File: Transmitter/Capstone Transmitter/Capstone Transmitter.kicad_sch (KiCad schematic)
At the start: 38 parts, among them J1 Conn_01x04, J2 Conn_01x04, J3 Conn_01x02_Socket, J4 Conn_01x02_Socket, J5 Conn_01x02_Socket, J6 AnalogStick Pot1 +/-, J7 AnalogStick Pot2 +/-, Q1 RevPolProt, U2 TPS63020DSJR, U3 ESP32-WROOM-32UE

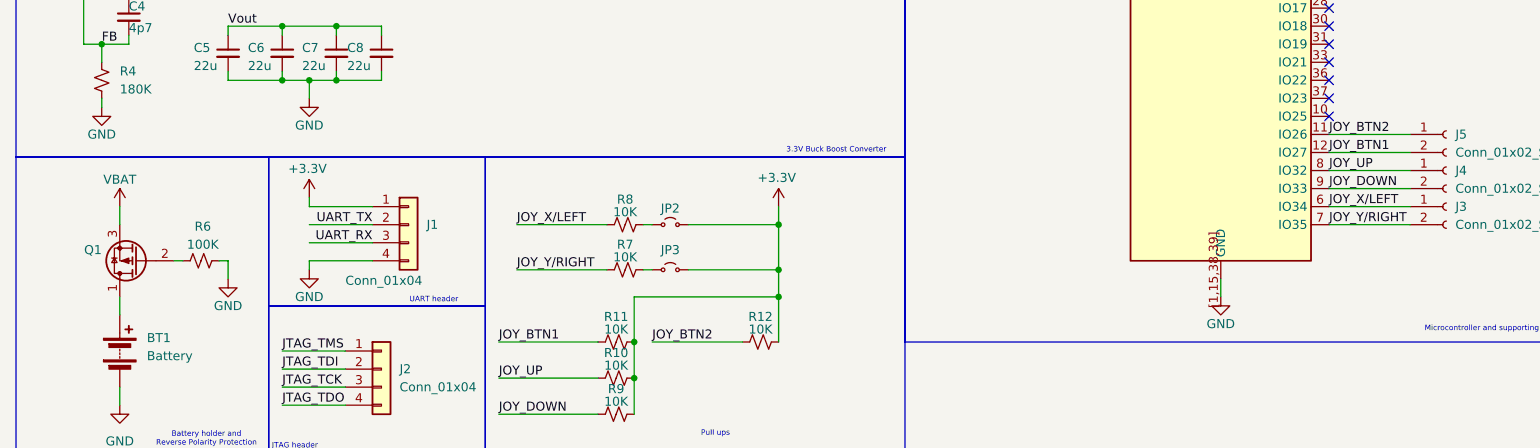
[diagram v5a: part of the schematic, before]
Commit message: Started PCB design with complete transmitter board. Please review
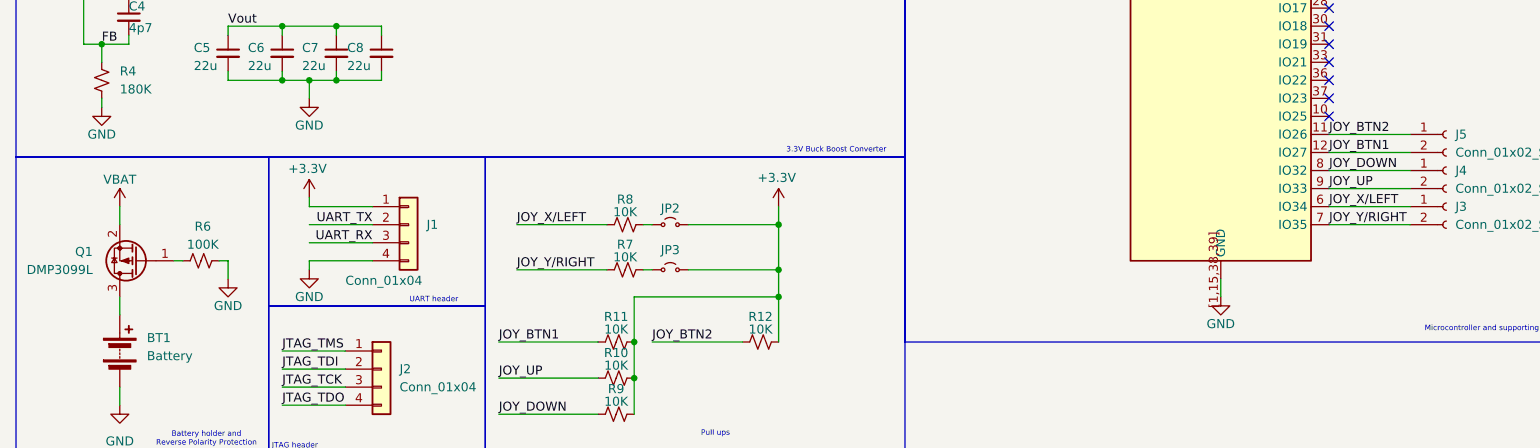
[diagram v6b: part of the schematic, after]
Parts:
- removed Q1: RevPolProt, symbol Transistor_FET:Q_PMOS_DGS
- added Q1: DMP3099L, Package_TO_SOT_SMD:SOT-23, symbol Transistor_FET:DMP3099L
- C1, C10, C11, C2, C4, C5, C6, C7, C8: footprint (none) -> Capacitor_SMD:C_0603_1608Metric
- C3, C9: footprint (none) -> Capacitor_SMD:C_0402_1005Metric
- J1, J2: footprint (none) -> Connector_PinHeader_2.54mm:PinHeader_1x04_P2.54mm_Vertical
- J3, J4, J5, J6, J7: footprint (none) -> TerminalBlock_CUI:TerminalBlock_CUI_TB007-508-02_1x02_P5.08mm_Horizontal
- JP1, JP2, JP3: footprint (none) -> Connector_PinHeader_2.54mm:PinHeader_1x02_P2.54mm_Vertical
- L1: footprint (none) -> Inductor_SMD_Wurth:L_Wurth_WE-LQSH-4020
- R1, R10, R11, R12, R2, R3, R4, R5, R6, R7, R8, R9: footprint (none) -> Resistor_SMD:R_0603_1608Metric
- U2: footprint DSJ14_2P85X1P58 -> footprints:DSJ14_2P85X1P58
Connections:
- net JOY_DOWN: now also J4.1 (Pin_1), U3.8 (IO32); no longer J4.2 (Pin_2), U3.9 (IO33)
- net JOY_UP: now also J4.2 (Pin_2), U3.9 (IO33); no longer J4.1 (Pin_1), U3.8 (IO32)
- net VBAT: now also Q1.2 (S)
- net at BT1.1 (+): now also Q1.3 (D)
- net at R6.1: now also Q1.1 (G)
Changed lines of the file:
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@@
 		)
 	)
-	(label "JOY_UP"
+	(label "JOY_DOWN"
 		(at 196.85 80.01 0)
 		(effects
@@
 		)
 	)
-	(label "JOY_DOWN"
+	(label "JOY_UP"
 		(at 196.85 82.55 0)
 		(effects
@@
 			)
 		)
-		(property "Footprint" ""
+		(property "Footprint" "Capacitor_SMD:C_0603_1608Metric"
 			(at 157.48 33.02 0)
 			(hide yes)
@@
 			)
 		)
-		(property "Footprint" ""
+		(property "Footprint" "TerminalBlock_CUI:TerminalBlock_CUI_TB007-508-02_1x02_P5.08mm_Horizontal"
 			(at 27.94 124.46 0)
 			(hide yes)
@@
 			)
 		)
-		(property "Footprint" ""
+		(property "Footprint" "Capacitor_SMD:C_0402_1005Metric"
 			(at 142.24 21.59 0)
 			(hide yes)
@@
 			)
 		)
-		(property "Footprint" ""
+		(property "Footprint" "Capacitor_SMD:C_0603_1608Metric"
 			(at 49.53 63.5 0)
 			(hide yes)
@@
 			)
 		)
-		(property "Footprint" ""
+		(property "Footprint" "Capacitor_SMD:C_0402_1005Metric"
 			(at 24.13 31.75 0)
 			(hide yes)
@@
 			)
 		)
-		(property "Footprint" ""
+		(property "Footprint" "Capacitor_SMD:C_0603_1608Metric"
 			(at 63.5 63.5 0)
 			(hide yes)
@@
 			)
 		)
-		(property "Footprint" ""
+		(property "Footprint" "Resistor_SMD:R_0603_1608Metric"
 			(at 96.52 109.22 0)
 			(hide yes)
@@
 			)
 		)
-		(property "Footprint" ""
+		(property "Footprint" "Connector_PinHeader_2.54mm:PinHeader_1x04_P2.54mm_Vertical"
 			(at 63.5 107.95 0)
 			(hide yes)
@@
 			)
 		)
-		(property "Footprint" ""
+		(property "Footprint" "TerminalBlock_CUI:TerminalBlock_CUI_TB007-508-02_1x02_P5.08mm_Horizontal"
 			(at 213.36 80.01 0)
 			(hide yes)
@@
 			)
 		)
-		(property "Footprint" ""
+		(property "Footprint" "Connector_PinHeader_2.54mm:PinHeader_1x02_P2.54mm_Vertical"
 			(at 104.14 87.63 0)
 			(hide yes)
@@
 			)
 		)
-		(property "Footprint" ""
+		(property "Footprint" "Connector_PinHeader_2.54mm:PinHeader_1x02_P2.54mm_Vertical"
 			(at 209.55 29.21 0)
 			(hide yes)
@@
 	)
 	(symbol
-		(lib_id "Transistor_FET:Q_PMOS_DGS")
-		(at 29.21 92.71 180)
-		(unit 1)
-		(body_style 1)
-		(exclude_from_sim no)
-		(in_bom yes)
-		(on_board yes)
-		(in_pos_files yes)
-		(dnp no)
-		(property "Reference" "Q1"
-			(at 24.13 91.186 0)
-			(show_name no)
-			(do_not_autoplace no)
-			(effects
-				(font
-					(size 1.27 1.27)
-				)
-				(justify left)
-			)
-		)
-		(property "Value" "RevPolProt"
-			(at 23.876 92.964 0)
-			(hide yes)
-			(show_name no)
-			(do_not_autoplace no)
-			(effects
-				(font
-					(size 1.27 1.27)
-				)
-				(justify left)
-			)
-		)
-		(property "Footprint" ""
-			(at 24.13 95.25 0)
-			(hide yes)
-			(show_name no)
-			(do_not_autoplace no)
-			(effects
-				(font
-					(size 1.27 1.27)
-				)
-			)
-		)
-		(property "Datasheet" ""
-			(at 29.21 92.71 0)
-			(hide yes)
-			(show_name no)
-			(do_not_autoplace no)
-			(effects
-				(font
-					(size 1.27 1.27)
-				)
-			)
-		)
-		(property "Description" "P-MOSFET transistor, drain/gate/source"
-			(at 29.21 92.71 0)
-			(hide yes)
-			(show_name no)
-			(do_not_autoplace no)
-			(effects
-				(font
-					(size 1.27 1.27)
-				)
-			)
-		)
-		(pin "2"
-		)
-		(pin "3"
-		)
-		(pin "1"
-		)
-		(instances
-			(project "Capstone Transmitter"
-				(path "/c6281f45-9be9-4db0-bb6a-14da59dc6c3d"
-					(reference "Q1")
-					(unit 1)
-				)
-			)
-		)
-	)
-	(symbol
 		(lib_id "power:+3.3V")
 		(at 20.32 123.19 0)
@@
 			)
 		)
-		(property "Footprint" ""
+		(property "Footprint" "Resistor_SMD:R_0603_1608Metric"
 			(at 27.94 50.8 0)
 			(hide yes)
@@
 			)
 		)
-		(property "Footprint" ""
+		(property "Footprint" "Inductor_SMD_Wurth:L_Wurth_WE-LQSH-4020"
 			(at 71.12 55.88 0)
 			(hide yes)
@@
 			)
 		)
-		(property "Footprint" ""
+		(property "Footprint" "Capacitor_SMD:C_0603_1608Metric"
 			(at 27.94 58.42 0)
 			(hide yes)
@@
 			)
 		)
-		(property "Footprint" ""
+		(property "Footprint" "Resistor_SMD:R_0603_1608Metric"
 			(at 24.13 67.31 0)
 			(hide yes)
@@
 			)
 		)
-		(property "Footprint" ""
+		(property "Footprint" "Resistor_SMD:R_0603_1608Metric"
 			(at 21.59 50.8 0)
 			(hide yes)
@@
 			)
 		)
-		(property "Footprint" ""
+		(property "Footprint" "Resistor_SMD:R_0603_1608Metric"
 			(at 96.52 114.3 0)
 			(hide yes)
@@
 			)
 		)
-		(property "Footprint" ""
+		(property "Footprint" "Resistor_SMD:R_0603_1608Metric"
 			(at 97.79 87.63 0)
 			(hide yes)
@@
 			)
 		)
-		(property "Footprint" ""
+		(property "Footprint" "Connector_PinHeader_2.54mm:PinHeader_1x02_P2.54mm_Vertical"
 			(at 104.14 93.98 0)
 			(hide yes)
@@
 	)
 	(symbol
+		(lib_id "Transistor_FET:DMP3099L")
+		(at 29.21 92.71 180)
+		(unit 1)
+		(body_style 1)
+		(exclude_from_sim no)
+		(in_bom yes)
+		(on_board yes)
+		(in_pos_files yes)
+		(dnp no)
+		(fields_autoplaced yes)
+		(property "Reference" "Q1"
+			(at 22.86 91.4399 0)
+			(show_name no)
+			(do_not_autoplace no)
+			(effects
+				(font
+					(size 1.27 1.27)
+				)
+				(justify left)
+			)
+		)
+		(property "Value" "DMP3099L"
+			(at 22.86 93.9799 0)
+			(show_name no)
+			(do_not_autoplace no)
+			(effects
+				(font
+					(size 1.27 1.27)
+				)
+				(justify left)
+			)
+		)
+		(property "Footprint" "Package_TO_SOT_SMD:SOT-23"
+			(at 24.13 90.805 0)
+			(hide yes)
+			(show_name no)
+			(do_not_autoplace no)
+			(effects
+				(font
+					(size 1.27 1.27)
+					(italic yes)
+				)
+				(justify left)
+			)
+		)
+		(property "Datasheet" "https://www.diodes.com/assets/Datasheets/DMP3099L.pdf"
+			(at 24.13 88.9 0)
+			(hide yes)
+			(show_name no)
+			(do_not_autoplace no)
+			(effects
+				(font
+					(size 1.27 1.27)
+				)
+				(justify left)
+			)
+		)
+		(property "Description" "-3.8A Id, -30V Vds, P-Channel MOSFET, SOT-23"
+			(at 29.21 92.71 0)
+			(hide yes)
+			(show_name no)
+			(do_not_autoplace no)
+			(effects
+				(font
+					(size 1.27 1.27)
+				)
+			)
+		)
+		(pin "1"
+		)
+		(pin "2"
+		)
+		(pin "3"
+		)
+		(instances
+			(project "Capstone Transmitter"
+				(path "/c6281f45-9be9-4db0-bb6a-14da59dc6c3d"
+					(reference "Q1")
+					(unit 1)
+				)
+			)
+		)
+	)
+	(symbol
 		(lib_id "power:+3.3V")
 		(at 27.94 46.99 0)
@@
 			)
 		)
-		(property "Footprint" ""
+		(property "Footprint" "TerminalBlock_CUI:TerminalBlock_CUI_TB007-508-02_1x02_P5.08mm_Horizontal"
 			(at 213.36 85.09 0)
 			(hide yes)
@@
 			)
 		)
-		(property "Footprint" ""
+		(property "Footprint" "Resistor_SMD:R_0603_1608Metric"
 			(at 96.52 104.14 0)
 			(hide yes)
@@
 			)
 		)
-		(property "Footprint" ""
+		(property "Footprint" "Resistor_SMD:R_0603_1608Metric"
 			(at 38.1 92.71 0)
 			(hide yes)
@@
 			)
 		)
-		(property "Footprint" ""
+		(property "Footprint" "Capacitor_SMD:C_0603_1608Metric"
 			(at 41.91 63.5 0)
 			(hide yes)
@@
 			)
 		)
-		(property "Footprint" ""
+		(property "Footprint" "TerminalBlock_CUI:TerminalBlock_CUI_TB007-508-02_1x02_P5.08mm_Horizontal"
 			(at 27.94 132.08 0)
 			(hide yes)
@@
 			)
 		)
-		(property "Footprint" ""
+		(property "Footprint" "Connector_PinHeader_2.54mm:PinHeader_1x04_P2.54mm_Vertical"
 			(at 67.31 87.63 0)
 			(hide yes)
@@
 			)
 		)
-		(property "Footprint" ""
+		(property "Footprint" "Resistor_SMD:R_0603_1608Metric"
 			(at 116.84 104.14 0)
 			(hide yes)
@@
 			)
 		)
-		(property "Footprint" ""
+		(property "Footprint" "Capacitor_SMD:C_0603_1608Metric"
 			(at 113.03 38.1 0)
 			(hide yes)
@@
 			)
 		)
-		(property "Footprint" ""
+		(property "Footprint" "Resistor_SMD:R_0603_1608Metric"
 			(at 157.48 24.13 0)
 			(hide yes)
@@
 			)
 		)
-		(property "Footprint" ""
+		(property "Footprint" "Resistor_SMD:R_0603_1608Metric"
 			(at 118.11 27.94 0)
 			(hide yes)
@@
 			)
 		)
-		(property "Footprint" ""
+		(property "Footprint" "Capacitor_SMD:C_0603_1608Metric"
 			(at 120.65 38.1 0)
 			(hide yes)
@@
 			)
 		)
-		(property "Footprint" "DSJ14_2P85X1P58"
+		(property "Footprint" "footprints:DSJ14_2P85X1P58"
 			(at 39.37 25.4 0)
 			(hide yes)
@@
 			)
 		)
-		(property "Footprint" ""
+		(property "Footprint" "Resistor_SMD:R_0603_1608Metric"
 			(at 97.79 93.98 0)
 			(hide yes)
@@
 			)
 		)
-		(property "Footprint" ""
+		(property "Footprint" "Capacitor_SMD:C_0603_1608Metric"
 			(at 57.15 63.5 0)
 			(hide yes)
@@
 			)
 		)
-		(property "Footprint" ""
+		(property "Footprint" "Capacitor_SMD:C_0603_1608Metric"
 			(at 149.86 21.59 0)
 			(hide yes)
@@
 			)
 		)
-		(property "Footprint" ""
+		(property "Footprint" "TerminalBlock_CUI:TerminalBlock_CUI_TB007-508-02_1x02_P5.08mm_Horizontal"
 			(at 213.36 74.93 0)
 			(hide yes)

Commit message: Removed convoluted battery power routing in exchange of DIN mounted AC-DC converter and DC-DC converter inputs
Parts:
- Q1: value DMP3099L -> DMP2035U
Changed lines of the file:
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@@
 			)
 		)
-		(property "Value" "DMP3099L"
+		(property "Value" "DMP2035U"
 			(at 22.86 93.9799 0)
 			(show_name no)

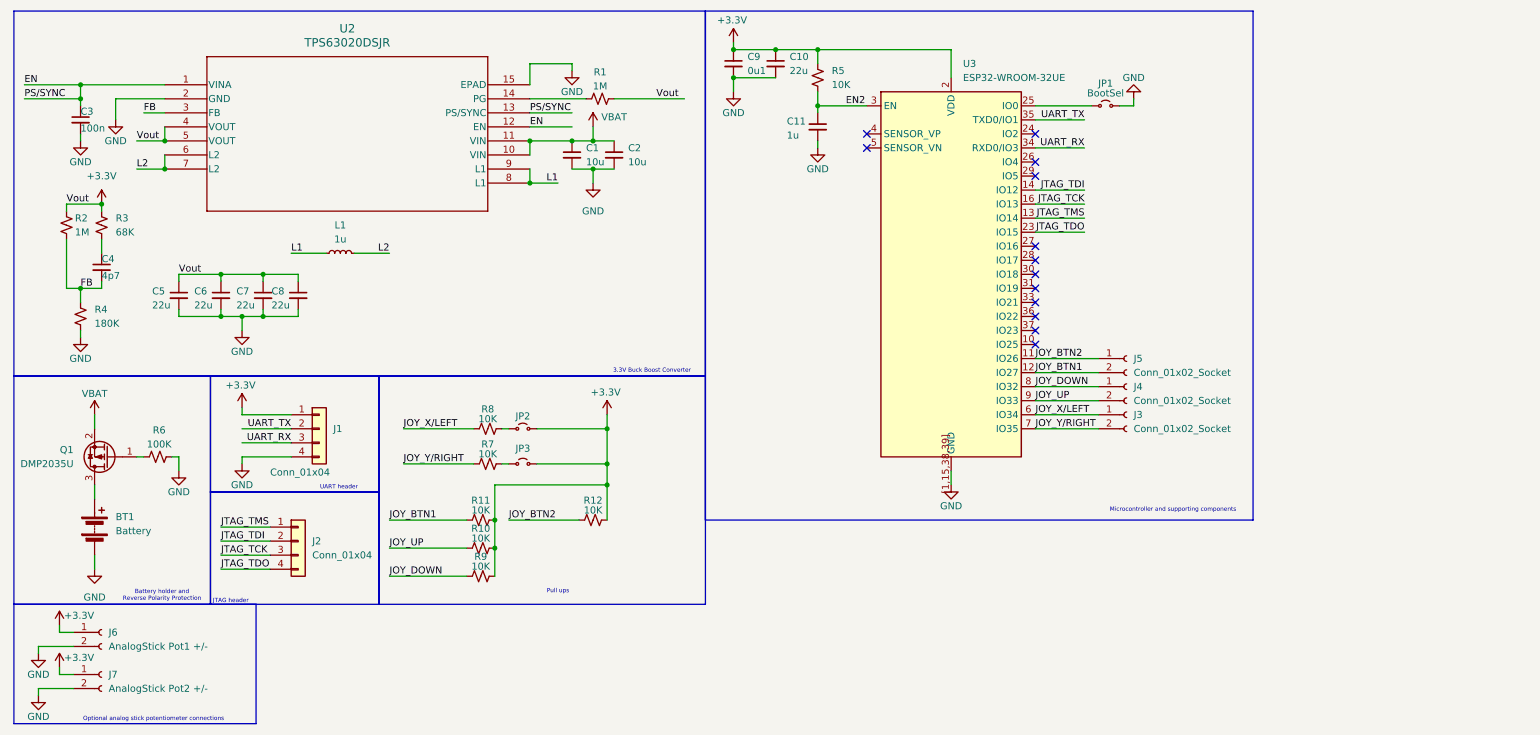
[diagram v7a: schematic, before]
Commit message: Moved battery around and added screw terminals for End of Travel (EoT) indicators
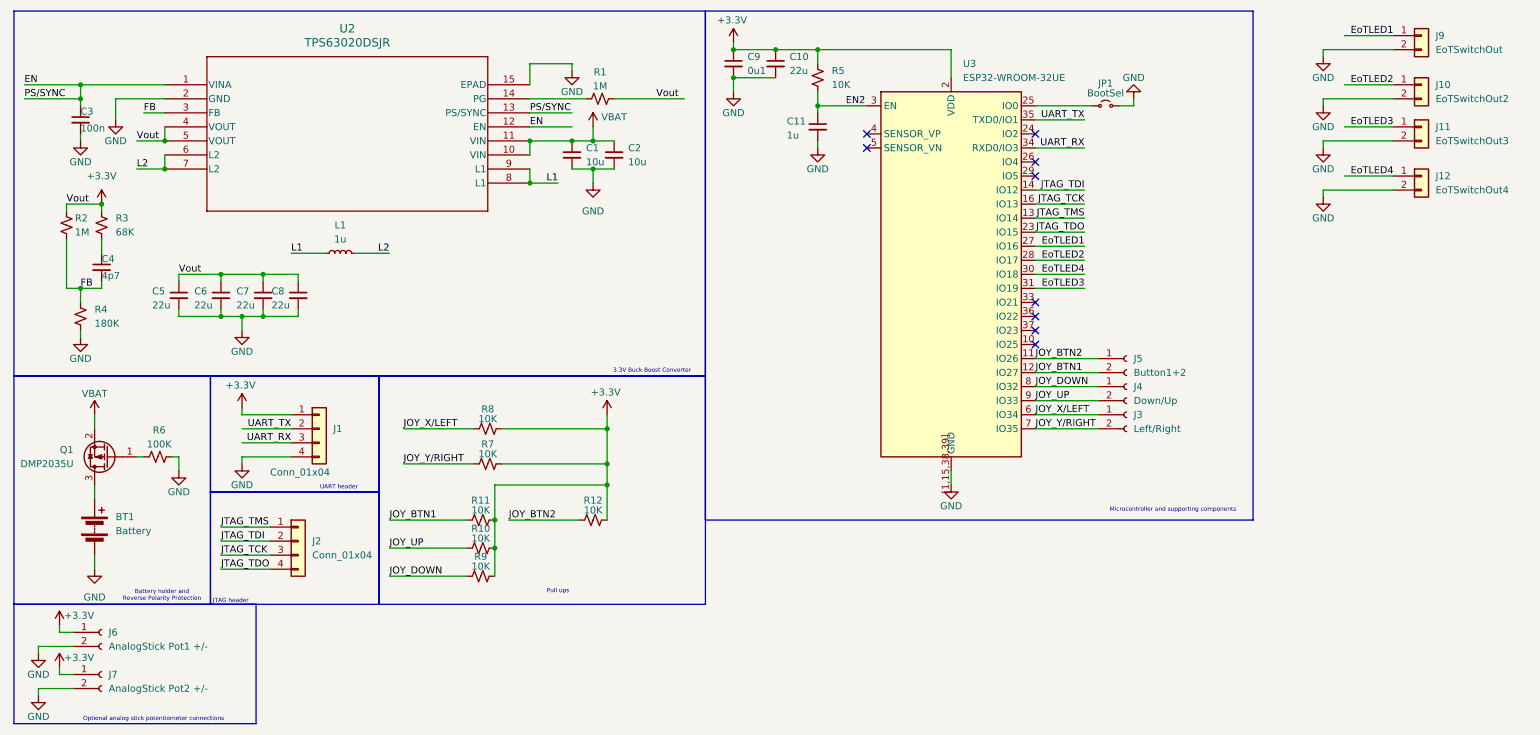
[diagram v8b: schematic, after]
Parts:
- removed JP2: Pull up Jumper 1, Connector_PinHeader_2.54mm:PinHeader_1x02_P2.54mm_Vertical, symbol Jumper:Jumper_2_Small_Open
- removed JP3: Pull up Jumper 2, Connector_PinHeader_2.54mm:PinHeader_1x02_P2.54mm_Vertical, symbol Jumper:Jumper_2_Small_Open
- added J10: EoTSwitchOut2, TerminalBlock_CUI:TerminalBlock_CUI_TB007-508-02_1x02_P5.08mm_Horizontal, symbol Connector_Generic:Conn_01x02
- added J11: EoTSwitchOut3, TerminalBlock_CUI:TerminalBlock_CUI_TB007-508-02_1x02_P5.08mm_Horizontal, symbol Connector_Generic:Conn_01x02
- added J12: EoTSwitchOut4, TerminalBlock_CUI:TerminalBlock_CUI_TB007-508-02_1x02_P5.08mm_Horizontal, symbol Connector_Generic:Conn_01x02
- added J9: EoTSwitchOut, TerminalBlock_CUI:TerminalBlock_CUI_TB007-508-02_1x02_P5.08mm_Horizontal, symbol Connector_Generic:Conn_01x02
- J3: value Conn_01x02_Socket -> Left/Right
- J4: value Conn_01x02_Socket -> Down/Up
- J5: value Conn_01x02_Socket -> Button1+2
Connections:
- net +3.3V: now also R7.2, R8.2
- net GND: now also J10.2 (Pin_2), J11.2 (Pin_2), J12.2 (Pin_2), J9.2 (Pin_2)
- net EoTLED1: now reaches U3.27 (IO16)
- net EoTLED1: now also J9.1 (Pin_1)
- net EoTLED2: now reaches U3.28 (IO17)
- net EoTLED2: now also J10.1 (Pin_1)
- net EoTLED4: now reaches U3.30 (IO18)
- net EoTLED4: now also J12.1 (Pin_1)
- net EoTLED3: now reaches U3.31 (IO19)
- net EoTLED3: now also J11.1 (Pin_1)
- no-connect marks 13 -> 9
